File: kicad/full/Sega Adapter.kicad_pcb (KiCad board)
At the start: 2 copper layers, 36.2 x 45.7 mm, 6 parts, among them J3 ICSP, U1 PIC16F1847

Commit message: Add KiCad projects for two adapter variants
The full adapter has an ICSP header for programming the PIC, a three-pin
jumper for C64/programming mode, and through-hole D-sub connectors.

The compact pcb removes the ICSP header but still has through-hole
connectors and a jumper for C64 mode.

The tiny pcb uses solder cup D-sub connectors and has a simple solder
bridge jumper for C64 mode.
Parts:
- moved C1 7.50 mm to (160.0, 115.6), turned to 180 degrees
- renumbered SEGA to J1, Atari to J2
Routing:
- net +5V: track 79.8 -> 74.7 mm
- net Net-(J2-Pad9): track 28.8 -> 29.5 mm

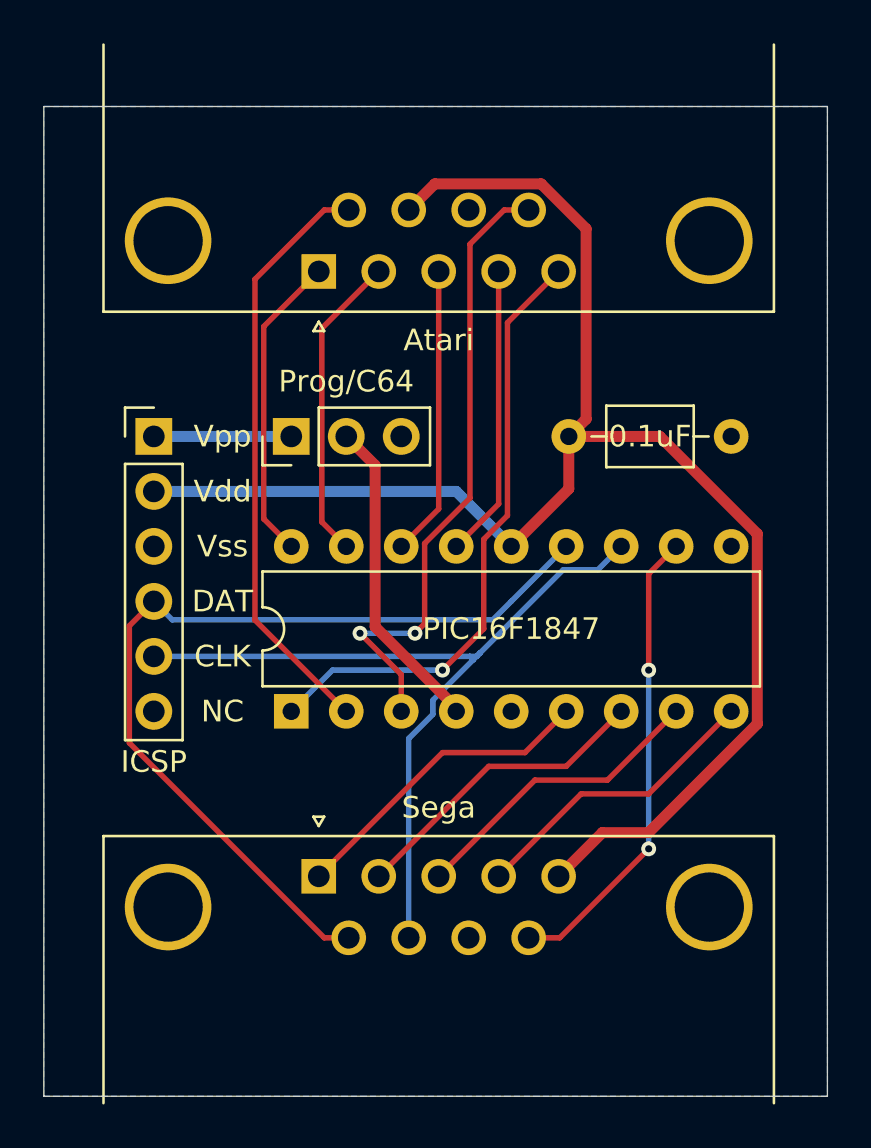
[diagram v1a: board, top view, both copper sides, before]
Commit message: Add README and licence
Also tweak the PCBs:
- round the corners of the full PCB
- add a copyright message to the full and tiny PCBs
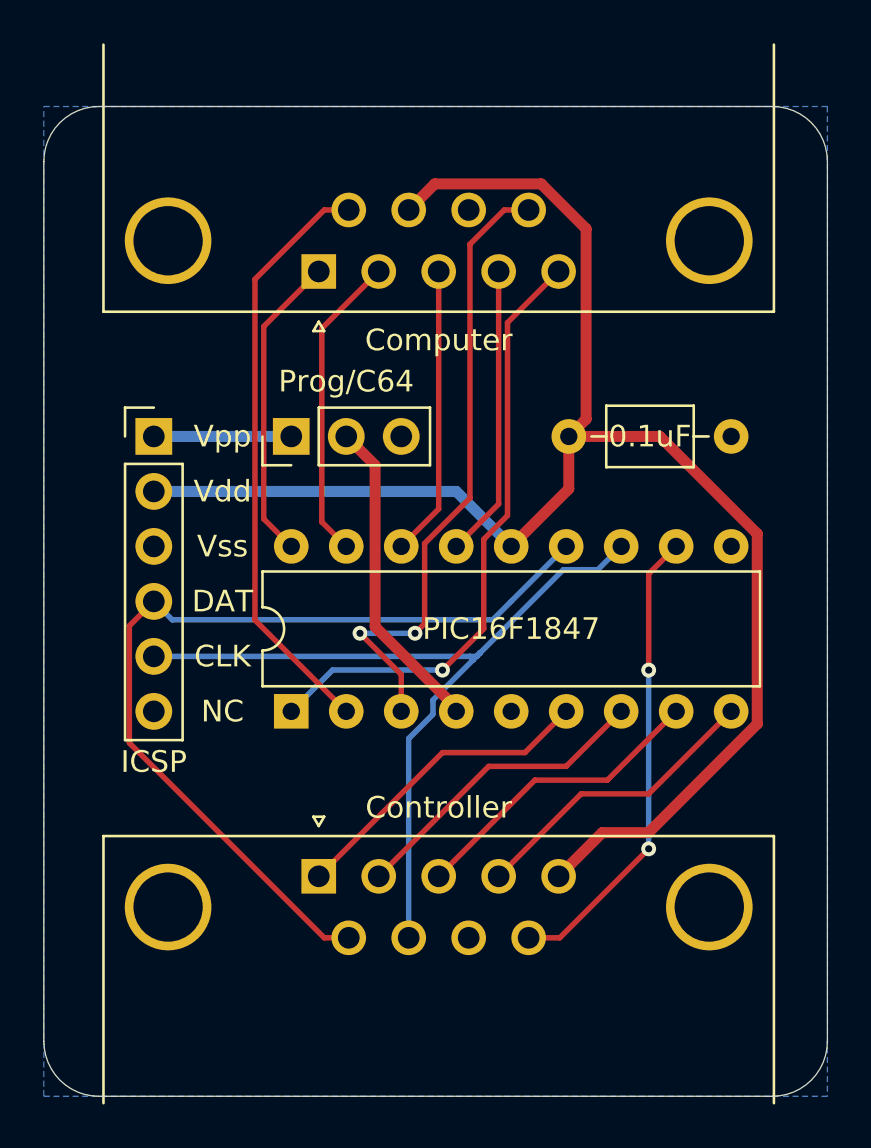
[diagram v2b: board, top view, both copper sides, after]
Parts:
- J1: value Sega -> Controller
- J2: value Atari -> Computer
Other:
- outline, holes or cut-outs redrawn
- board text added: "Sega Controller Adapter Copyright © 2021 Eyvind Bernhardsen"
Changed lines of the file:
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@@
   (general
     (thickness 1.6)
-    (drawings 10)
+    (drawings 15)
     (tracks 95)
     (zones 0)
@@
       (effects (font (size 1 1) (thickness 0.15)))
     )
-    (fp_text value Atari (at -5.54 -3.175) (layer F.SilkS)
+    (fp_text value Computer (at -5.54 -3.175) (layer F.SilkS)
       (effects (font (size 1 1) (thickness 0.15)))
     )
@@
       (effects (font (size 1 1) (thickness 0.15)))
     )
-    (fp_text value Sega (at 5.54 -3.175) (layer F.SilkS)
+    (fp_text value Controller (at 5.54 -3.175) (layer F.SilkS)
       (effects (font (size 1 1) (thickness 0.15)))
     )
@@
     )
   )
+  (gr_text "Sega Controller Adapter\nCopyright © 2021 Eyvind Bernhardsen" (at 146.685 142.875) (layer B.SilkS)
+    (effects (font (size 1 1) (thickness 0.15)) (justify mirror))
+  )
+  (gr_line (start 130.81 100.33) (end 161.925 100.33) (layer Edge.Cuts) (width 0.05))
+  (gr_line (start 128.27 143.51) (end 128.27 102.87) (layer Edge.Cuts) (width 0.05))
+  (gr_line (start 161.925 146.05) (end 130.81 146.05) (layer Edge.Cuts) (width 0.05))
+  (gr_line (start 164.465 102.87) (end 164.465 143.51) (layer Edge.Cuts) (width 0.05))
+  (gr_arc (start 130.81 143.51) (end 128.27 143.51) (angle -90) (layer Edge.Cuts) (width 0.05))
+  (gr_arc (start 161.925 143.51) (end 161.925 146.05) (angle -90) (layer Edge.Cuts) (width 0.05))
+  (gr_arc (start 161.925 102.87) (end 164.465 102.87) (angle -90) (layer Edge.Cuts) (width 0.05))
+  (gr_arc (start 130.81 102.87) (end 130.81 100.33) (angle -90) (layer Edge.Cuts) (width 0.05))
   (gr_text NC (at 136.525 128.27) (layer F.SilkS)
     (effects (font (size 1 1) (thickness 0.15)))
@@
     (effects (font (size 1 1) (thickness 0.15)))
   )
-  (gr_line (start 164.465 146.05) (end 128.27 146.05) (layer Edge.Cuts) (width 0.05))
-  (gr_line (start 128.27 100.33) (end 164.465 100.33) (layer Edge.Cuts) (width 0.05))
-  (gr_line (start 164.465 100.33) (end 164.465 146.05) (layer Edge.Cuts) (width 0.05))
-  (gr_line (start 128.27 100.33) (end 128.27 146.05) (layer Edge.Cuts) (width 0.05))
   (segment (start 152.4 128.27) (end 150.495 130.175) (width 0.254) (layer F.Cu) (net 1))
   (segment (start 146.685 130.175) (end 140.97 135.89) (width 0.254) (layer F.Cu) (net 1))
